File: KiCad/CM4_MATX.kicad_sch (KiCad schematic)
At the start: 9 parts

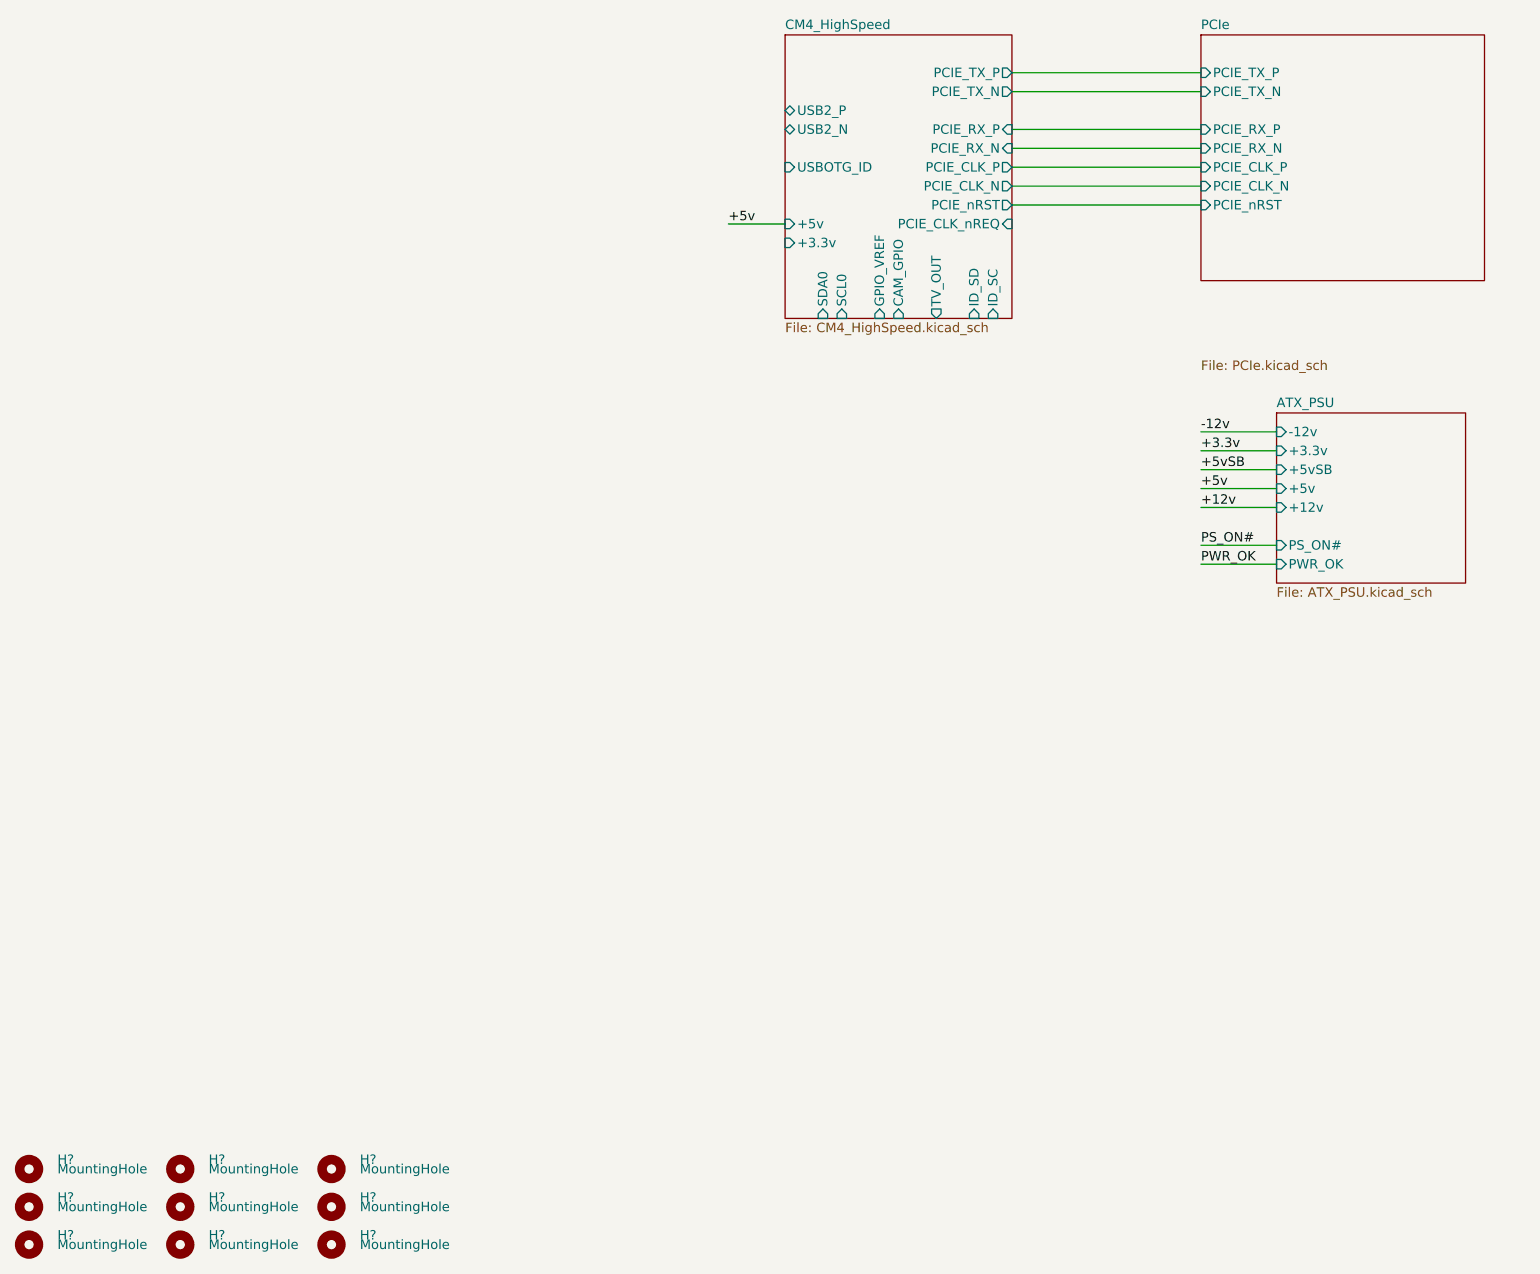
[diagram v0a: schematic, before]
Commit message: Big changes (see expanded comment)
Added new components:
USB2517-JZX USB2.0 Hub
SI-52100-002 Vertical USB2.0 A Header

Began work on USB schematic, mostly done. Needs power delivery work done
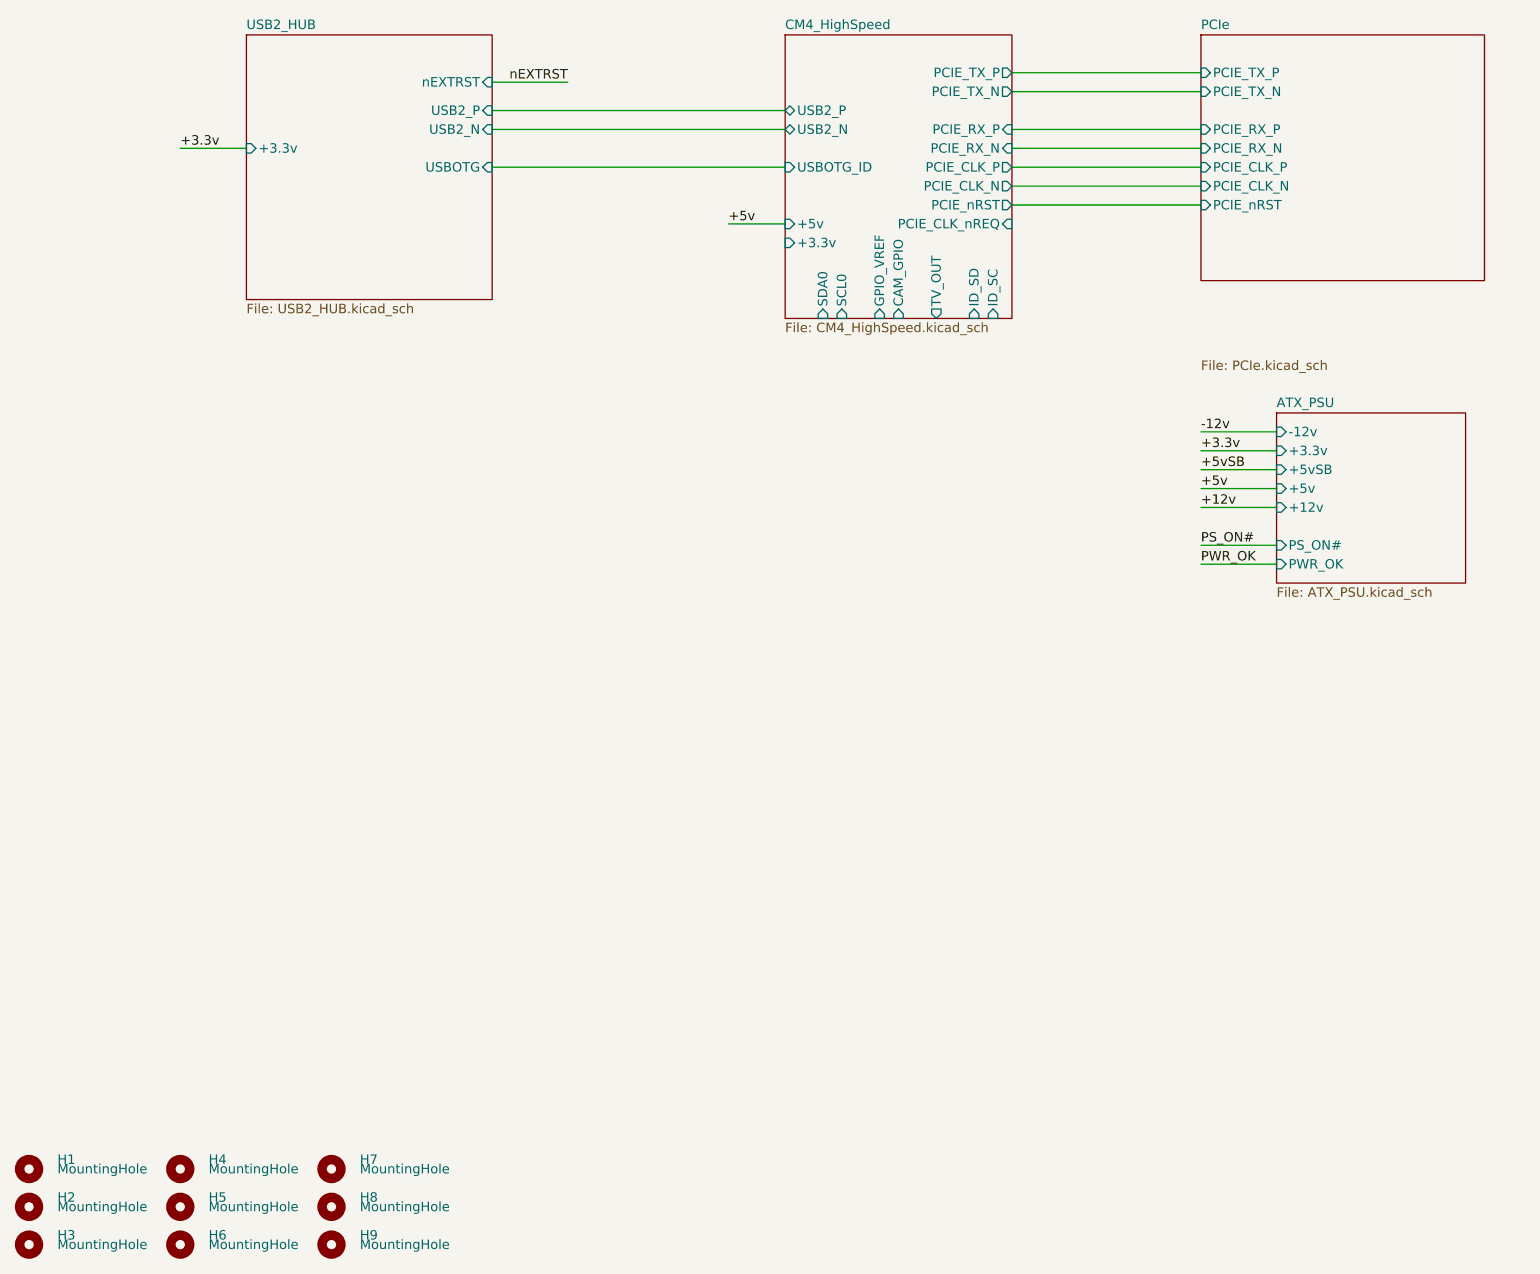
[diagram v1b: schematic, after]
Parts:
- H1, H2, H3, H4, H5, H6, H7, H8, H9: renamed from H?; footprint (none) -> MountingHole:MountingHole_3.2mm_M3
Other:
- added sheet USB2_HUB (USB2_HUB.kicad_sch)
- company: (none) -> TheGuyDanish
- title: (none) -> Raspberry Pi CM4 mATX Motherboard

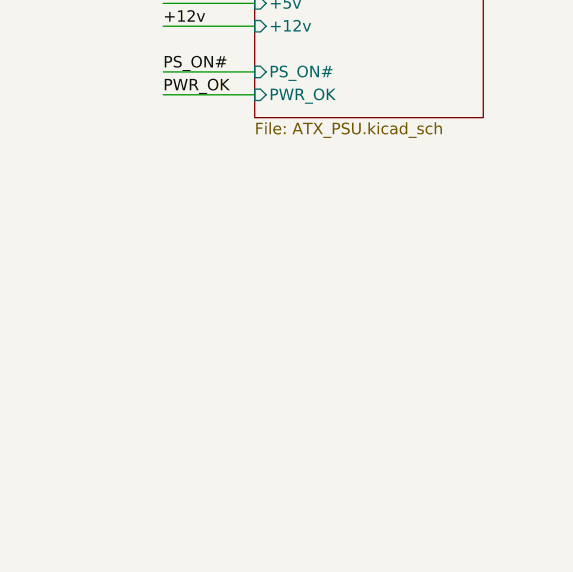
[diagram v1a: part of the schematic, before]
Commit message: added CM4_FanCRTL to CM4_MATX
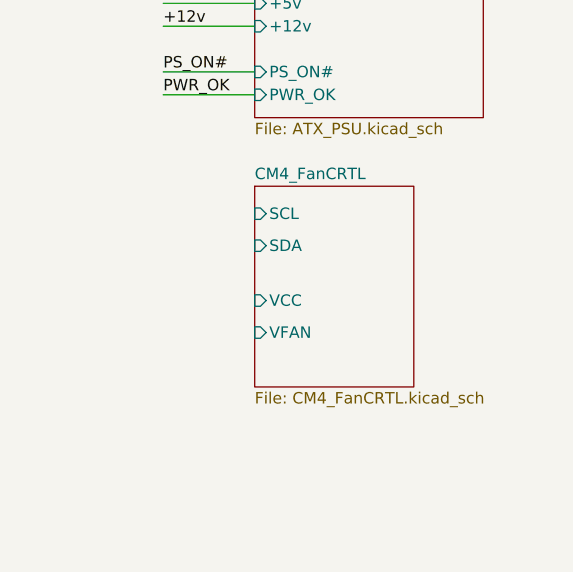
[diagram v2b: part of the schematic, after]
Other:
- added sheet CM4_FanCRTL (CM4_FanCRTL.kicad_sch)
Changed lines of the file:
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@@
-(kicad_sch (version 20200828) (generator eeschema)
-  (page 1 5)
+(kicad_sch (version 20201015) (generator eeschema)
+  (page 1 6)
   (paper "A4")
   (title_block
@@
     )
   )
+  (sheet (at 193.04 106.68) (size 17.6784 22.3012)
+    (stroke (width 0.001) (type solid) (color 132 0 132 1))
+    (fill (color 255 255 255 0.0000))
+    (property "Sheet name" "CM4_FanCRTL" (id 0) (at 193.04 106.0441 0)
+      (effects (font (size 1.27 1.27)) (justify left bottom))
+    )
+    (property "Sheet file" "CM4_FanCRTL.kicad_sch" (id 1) (at 193.04 129.4901 0)
+      (effects (font (size 1.27 1.27)) (justify left top))
+    )
+    (pin "SCL" input (at 193.04 109.728 180)
+      (effects (font (size 1.27 1.27)) (justify left))
+    )
+    (pin "VCC" input (at 193.04 119.38 180)
+      (effects (font (size 1.27 1.27)) (justify left))
+    )
+    (pin "SDA" input (at 193.04 113.284 180)
+      (effects (font (size 1.27 1.27)) (justify left))
+    )
+    (pin "VFAN" input (at 193.04 122.936 180)
+      (effects (font (size 1.27 1.27)) (justify left))
+    )
+  )
   (sheet (at 127 25.4) (size 30.48 38.1)
     (stroke (width 0.001) (type solid) (color 132 0 132 1))
@@
     )
   )
+  (sheet_instances
+    (path "/" (page "1"))
+    (path "/bc607ef6-2e5d-48f8-97ec-15102c5700ee/" (page "2"))
+    (path "/7df5f1b5-9b16-4444-96e6-6b5fbf7bb6cb/" (page "3"))
+    (path "/28df4f8e-5c71-4877-b43d-e34bce48f8bf/" (page "4"))
+    (path "/c5832ff1-3011-438e-bda2-1e0d07aa3027/" (page "5"))
+    (path "/26c1d330-8bac-4588-a428-2f7ba26a87a8/" (page "6"))
+  )
   (symbol_instances
     (path "/cca0c942-de3f-4419-8ac9-dcdd127758e3"
@@
       (reference "J9") (unit 1) (value "39-28-1243") (footprint "SHDR24W125P550X420_2X12_5160X960X1310P")
     )
-  )
+    (path "/26c1d330-8bac-4588-a428-2f7ba26a87a8/4662baa8-ce6a-4f3f-b06b-bebb2af10d70"
+      (reference "#PWR0133") (unit 1) (value "GND") (footprint "")
+    )
+    (path "/26c1d330-8bac-4588-a428-2f7ba26a87a8/d127651c-83de-4cd5-8915-0efe9292e0ce"
+      (reference "#PWR0134") (unit 1) (value "GND") (footprint "")
+    )
+    (path "/26c1d330-8bac-4588-a428-2f7ba26a87a8/dd97aa89-e6c1-467b-a330-94d2fa31fc25"
+      (reference "#PWR0135") (unit 1) (value "VCC") (footprint "")
+    )
+    (path "/26c1d330-8bac-4588-a428-2f7ba26a87a8/2d4cac26-140d-4f09-9602-ee01c04cfb47"
+      (reference "#PWR0136") (unit 1) (value "GND") (footprint "")
+    )
+    (path "/26c1d330-8bac-4588-a428-2f7ba26a87a8/49bcada2-3d64-4b54-b171-36db3aa442ae"
+      (reference "#PWR0137") (unit 1) (value "VCC") (footprint "")
+    )
+    (path "/26c1d330-8bac-4588-a428-2f7ba26a87a8/3099f062-beae-475a-b289-24dca11649a8"
+      (reference "#PWR0138") (unit 1) (value "VCC") (footprint "")
+    )
+    (path "/26c1d330-8bac-4588-a428-2f7ba26a87a8/a7d85335-d339-49b6-a79c-9011e277622c"
+      (reference "#PWR0139") (unit 1) (value "GND") (footprint "")
+    )
+    (path "/26c1d330-8bac-4588-a428-2f7ba26a87a8/acc98e54-61df-4bce-b2e9-d92586289983"
+      (reference "#PWR0140") (unit 1) (value "GND") (footprint "")
+    )
+    (path "/26c1d330-8bac-4588-a428-2f7ba26a87a8/4d40647b-4ee8-4e67-9379-d27ea23ac342"
+      (reference "#TACH11") (unit 1) (value "TACH1") (footprint "")
+    )
+    (path "/26c1d330-8bac-4588-a428-2f7ba26a87a8/b0778758-e177-41ea-94af-b86b12d685a3"
+      (reference "#TACH12") (unit 1) (value "TACH1") (footprint "")
+    )
+    (path "/26c1d330-8bac-4588-a428-2f7ba26a87a8/c6d65c30-eccf-4427-a362-5725a21cc517"
+      (reference "#TACH21") (unit 1) (value "TACH2") (footprint "")
+    )
+    (path "/26c1d330-8bac-4588-a428-2f7ba26a87a8/325fd72b-1686-4226-8f3d-e50f7787374a"
+      (reference "#TACH22") (unit 1) (value "TACH2") (footprint "")
+    )
+    (path "/26c1d330-8bac-4588-a428-2f7ba26a87a8/8486454f-159a-43e5-9482-af42b8441592"
+      (reference "#VREF0101") (unit 1) (value "VREF") (footprint "")
+    )
+    (path "/26c1d330-8bac-4588-a428-2f7ba26a87a8/c52cae68-af4f-41a2-beea-2417b3af1635"
+      (reference "#VREF0102") (unit 1) (value "VREF") (footprint "")
+    )
+    (path "/26c1d330-8bac-4588-a428-2f7ba26a87a8/b2d656af-3fe1-4964-a0a2-6f275092a33e"
+      (reference "C13") (unit 1) (value "C100p") (footprint "CM4_MATX:C_0805_2012Metric")
+    )
+    (path "/26c1d330-8bac-4588-a428-2f7ba26a87a8/a266e41e-0ff1-4c54-a0e5-d09ca8dab726"
+      (reference "C14") (unit 1) (value "C100p") (footprint "CM4_MATX:C_0805_2012Metric")
+    )
+    (path "/26c1d330-8bac-4588-a428-2f7ba26a87a8/3d232897-b634-43ac-a725-2c5a2d697f20"
+      (reference "C15") (unit 1) (value "C0.1u") (footprint "CM4_MATX:C_0805_2012Metric")
+    )
+    (path "/26c1d330-8bac-4588-a428-2f7ba26a87a8/9608a344-c1b3-4f8d-9337-d16fa7b6db60"
+      (reference "J14") (unit 1) (value "KK-254-470531000") (footprint "CM4_MATX:Molex_KK-254_AE-6410-04A_1x04_P2.54mm_Vertical")
+    )
+    (path "/26c1d330-8bac-4588-a428-2f7ba26a87a8/02e5836f-708b-4da5-b249-dcff5ee907bb"
+      (reference "J15") (unit 1) (value "KK-254-470531000") (footprint "CM4_MATX:Molex_KK-254_AE-6410-04A_1x04_P2.54mm_Vertical")
+    )
+    (path "/26c1d330-8bac-4588-a428-2f7ba26a87a8/634a670f-9345-4af7-bab3-20081028da94"
+      (reference "JP1") (unit 1) (value "SolderJumper_2_Open") (footprint "CM4_MATX:R_0805_2012Metric")
+    )
+    (path "/26c1d330-8bac-4588-a428-2f7ba26a87a8/03c60bfc-ab71-49c9-8af2-3535d3ed8169"
+      (reference "JP2") (unit 1) (value "SolderJumper_2_Open") (footprint "CM4_MATX:R_0805_2012Metric")
+    )
+    (path "/26c1d330-8bac-4588-a428-2f7ba26a87a8/40a4a595-c9b8-4906-80c2-cfabac498d5b"
+      (reference "R9") (unit 1) (value "R1.6k") (footprint "CM4_MATX:R_0805_2012Metric")
+    )
+    (path "/26c1d330-8bac-4588-a428-2f7ba26a87a8/3e570b74-ef48-488d-b902-8cd1711517e2"
+      (reference "R10") (unit 1) (value "R1.6k") (footprint "CM4_MATX:R_0805_2012Metric")
+    )
+    (path "/26c1d330-8bac-4588-a428-2f7ba26a87a8/6baffab2-cc53-4bb4-89f3-6d03df6fcf9a"
+      (reference "R11") (unit 1) (value "R10k") (footprint "CM4_MATX:R_0805_2012Metric")
+    )
+    (path "/26c1d330-8bac-4588-a428-2f7ba26a87a8/d0107591-f9b7-4686-a872-7af03327e26a"
+      (reference "R12") (unit 1) (value "R10k") (footprint "CM4_MATX:R_0805_2012Metric")
+    )
+    (path "/26c1d330-8bac-4588-a428-2f7ba26a87a8/058f3ee1-2f9a-4b2b-ae10-1dc65958a26b"
+      (reference "R13") (unit 1) (value "R4.7k") (footprint "CM4_MATX:R_0805_2012Metric")
+    )
+    (path "/26c1d330-8bac-4588-a428-2f7ba26a87a8/7d84369f-b926-4c8f-addc-5eb965925f04"
+      (reference "R14") (unit 1) (value "R4.7k") (footprint "CM4_MATX:R_0805_2012Metric")
+    )
+    (path "/26c1d330-8bac-4588-a428-2f7ba26a87a8/4fad45df-e6c8-4ad0-af24-33671678dc2d"
+      (reference "U3") (unit 1) (value "MAX6615AEE+") (footprint "CM4_MATX:MAX6615AEE&plus_")
+    )
+  )
